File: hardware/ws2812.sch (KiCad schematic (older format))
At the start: 0 parts

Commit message: update,
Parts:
- added D?: WS2812, LED_SMD:LED_WS2812_PLCC6_5.0x5.0mm_P1.6mm, symbol LED:WS2812

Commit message: update,
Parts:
- gave numbers to parts that had none: 1
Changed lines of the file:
@@
 EESchema Schematic File Version 4
 LIBS:eval_board-cache
-LIBS:bb-ch340t-cache
 EELAYER 29 0
 EELAYER END
 $Descr A4 11693 8268
 encoding utf-8
-Sheet 8 20
+Sheet 8 22
 Title ""
 Date ""
@@
 $EndBitmap
 $Comp
-L LED:WS2812 D?
+L LED:WS2812 D1
 U 1 1 5CE91B05
 P 3650 3050
-F 0 "D?" H 4000 3100 50  0000 L CNN
+F 0 "D1" H 4000 3100 50  0000 L CNN
 F 1 "WS2812" H 4000 3050 50  0000 L CNN
 F 2 "LED_SMD:LED_WS2812_PLCC6_5.0x5.0mm_P1.6mm" H 3700 2750 50  0001 L TNN

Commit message: update,
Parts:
- added D? (x2): WS2812, LED_SMD:LED_WS2812_PLCC6_5.0x5.0mm_P1.6mm, symbol LED:WS2812
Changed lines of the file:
@@
 $Descr A4 11693 8268
 encoding utf-8
-Sheet 8 21
+Sheet 6 20
 Title ""
 Date ""
@@
 	1    0    0    -1
 $EndComp
+$Comp
+L LED:WS2812 D?
+U 1 1 5CF2390D
+P 4550 3050
+F 0 "D?" H 4900 3100 50  0000 L CNN
+F 1 "WS2812" H 4900 3050 50  0000 L CNN
+F 2 "LED_SMD:LED_WS2812_PLCC6_5.0x5.0mm_P1.6mm" H 4600 2750 50  0001 L TNN
+F 3 "https://cdn-shop.adafruit.com/datasheets/WS2812.pdf" H 4650 2675 50  0001 L TNN
+	1    4550 3050
+	1    0    0    -1
+$EndComp
+$Comp
+L LED:WS2812 D?
+U 1 1 5CF23CE3
+P 5400 3050
+F 0 "D?" H 5750 3100 50  0000 L CNN
+F 1 "WS2812" H 5750 3050 50  0000 L CNN
+F 2 "LED_SMD:LED_WS2812_PLCC6_5.0x5.0mm_P1.6mm" H 5450 2750 50  0001 L TNN
+F 3 "https://cdn-shop.adafruit.com/datasheets/WS2812.pdf" H 5500 2675 50  0001 L TNN
+	1    5400 3050
+	1    0    0    -1
+$EndComp

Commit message: update,
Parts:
- added U?: 74AHCT1G125, Package_TO_SOT_SMD:SOT-23-5_HandSoldering, symbol 74xGxx:74AHCT1G125
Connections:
- new net GND: U?.3 (GND)
- new net VCC: U?.5 (VCC)
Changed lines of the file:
@@
+	1    0    0    -1
+$EndComp
+$Comp
+L 74xGxx:74AHCT1G125 U?
+U 1 1 5CFAEDA6
+P 2450 3000
+F 0 "U?" H 2450 2750 50  0001 C CNN
+F 1 "74AHCT1G125" H 2450 2800 50  0000 C CNN
+F 2 "Package_TO_SOT_SMD:SOT-23-5_HandSoldering" H 2450 3000 50  0001 C CNN
+F 3 "http://www.ti.com/lit/sg/scyt129e/scyt129e.pdf" H 2450 3000 50  0001 C CNN
+	1    2450 3000
 	1    0    0    -1
 $EndComp

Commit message: update,
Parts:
- gave numbers to parts that had none: 3
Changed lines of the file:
@@
 $EndComp
 $Comp
-L LED:WS2812 D?
+L LED:WS2812 D8
 U 1 1 5CF2390D
 P 4550 3050
-F 0 "D?" H 4900 3100 50  0000 L CNN
+F 0 "D8" H 4900 3100 50  0000 L CNN
 F 1 "WS2812" H 4900 3050 50  0000 L CNN
 F 2 "LED_SMD:LED_WS2812_PLCC6_5.0x5.0mm_P1.6mm" H 4600 2750 50  0001 L TNN
@@
 $EndComp
 $Comp
-L LED:WS2812 D?
+L LED:WS2812 D9
 U 1 1 5CF23CE3
 P 5400 3050
-F 0 "D?" H 5750 3100 50  0000 L CNN
+F 0 "D9" H 5750 3100 50  0000 L CNN
 F 1 "WS2812" H 5750 3050 50  0000 L CNN
 F 2 "LED_SMD:LED_WS2812_PLCC6_5.0x5.0mm_P1.6mm" H 5450 2750 50  0001 L TNN
@@
 $EndComp
 $Comp
-L 74xGxx:74AHCT1G125 U?
+L 74xGxx:74AHCT1G125 U7
 U 1 1 5CFAEDA6
 P 2450 3000
-F 0 "U?" H 2450 2750 50  0001 C CNN
+F 0 "U7" H 2450 2750 50  0001 C CNN
 F 1 "74AHCT1G125" H 2450 2800 50  0000 C CNN
 F 2 "Package_TO_SOT_SMD:SOT-23-5_HandSoldering" H 2450 3000 50  0001 C CNN

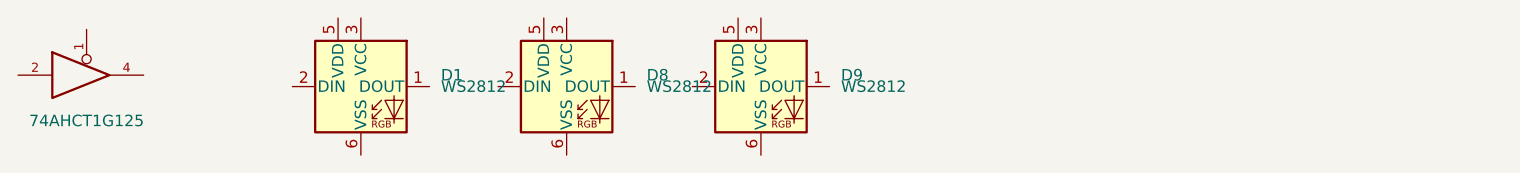
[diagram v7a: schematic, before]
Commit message: update for add capacitor,
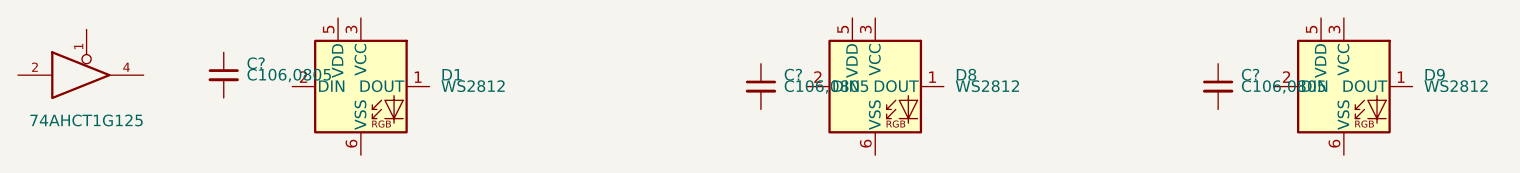
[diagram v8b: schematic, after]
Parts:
- added C? (x3): C106,0805, Capacitor_SMD:C_0805_2012Metric_Pad1.15x1.40mm_HandSolder, symbol taobao-c:C106,0805
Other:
- moved on the sheet: D8, D9
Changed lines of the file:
@@
 $Descr A4 11693 8268
 encoding utf-8
-Sheet 6 20
+Sheet 6 21
 Title ""
 Date ""
@@
 L LED:WS2812 D8
 U 1 1 5CF2390D
-P 4550 3050
-F 0 "D8" H 4900 3100 50  0000 L CNN
-F 1 "WS2812" H 4900 3050 50  0000 L CNN
-F 2 "LED_SMD:LED_WS2812_PLCC6_5.0x5.0mm_P1.6mm" H 4600 2750 50  0001 L TNN
-F 3 "https://cdn-shop.adafruit.com/datasheets/WS2812.pdf" H 4650 2675 50  0001 L TNN
-	1    4550 3050
+P 5900 3050
+F 0 "D8" H 6250 3100 50  0000 L CNN
+F 1 "WS2812" H 6250 3050 50  0000 L CNN
+F 2 "LED_SMD:LED_WS2812_PLCC6_5.0x5.0mm_P1.6mm" H 5950 2750 50  0001 L TNN
+F 3 "https://cdn-shop.adafruit.com/datasheets/WS2812.pdf" H 6000 2675 50  0001 L TNN
+	1    5900 3050
 	1    0    0    -1
 $EndComp
@@
 L LED:WS2812 D9
 U 1 1 5CF23CE3
-P 5400 3050
-F 0 "D9" H 5750 3100 50  0000 L CNN
-F 1 "WS2812" H 5750 3050 50  0000 L CNN
-F 2 "LED_SMD:LED_WS2812_PLCC6_5.0x5.0mm_P1.6mm" H 5450 2750 50  0001 L TNN
-F 3 "https://cdn-shop.adafruit.com/datasheets/WS2812.pdf" H 5500 2675 50  0001 L TNN
-	1    5400 3050
+P 7950 3050
+F 0 "D9" H 8300 3100 50  0000 L CNN
+F 1 "WS2812" H 8300 3050 50  0000 L CNN
+F 2 "LED_SMD:LED_WS2812_PLCC6_5.0x5.0mm_P1.6mm" H 8000 2750 50  0001 L TNN
+F 3 "https://cdn-shop.adafruit.com/datasheets/WS2812.pdf" H 8050 2675 50  0001 L TNN
+	1    7950 3050
 	1    0    0    -1
 $EndComp
@@
 	1    0    0    -1
 $EndComp
+$Comp
+L taobao-c:C106,0805 C?
+U 1 1 5CE4C478
+P 3050 3000
+F 0 "C?" H 3150 3050 50  0000 L CNN
+F 1 "C106,0805" H 3150 3000 50  0000 L CNN
+F 2 "Capacitor_SMD:C_0805_2012Metric_Pad1.15x1.40mm_HandSolder" H 3050 3000 50  0001 C CNN
+F 3 "~" H 3050 3000 50  0001 C CNN
+	1    3050 3000
+	1    0    0    -1
+$EndComp
+$Comp
+L taobao-c:C106,0805 C?
+U 1 1 5CE4D2A2
+P 5400 3050
+F 0 "C?" H 5500 3100 50  0000 L CNN
+F 1 "C106,0805" H 5500 3050 50  0000 L CNN
+F 2 "Capacitor_SMD:C_0805_2012Metric_Pad1.15x1.40mm_HandSolder" H 5400 3050 50  0001 C CNN
+F 3 "~" H 5400 3050 50  0001 C CNN
+	1    5400 3050
+	1    0    0    -1
+$EndComp
+$Comp
+L taobao-c:C106,0805 C?
+U 1 1 5CE4D6A6
+P 7400 3050
+F 0 "C?" H 7500 3100 50  0000 L CNN
+F 1 "C106,0805" H 7500 3050 50  0000 L CNN
+F 2 "Capacitor_SMD:C_0805_2012Metric_Pad1.15x1.40mm_HandSolder" H 7400 3050 50  0001 C CNN
+F 3 "~" H 7400 3050 50  0001 C CNN
+	1    7400 3050
+	1    0    0    -1
+$EndComp
